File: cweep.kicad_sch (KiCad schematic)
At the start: 73 parts, among them J1 24AWG Hole, J2 24AWG Hole, SW1 SW_Push, SW10 SW_Push, SW11 SW_Push, SW12 SW_Push, SW13 SW_Push, SW14 SW_Push, SW15 SW_Push, SW16 SW_Push, SW17 SW_Push, SW18 SW_SPST, SW19 SW_Omron_B3FS, SW2 SW_Push, SW3 SW_Push, SW4 SW_Push, SW5 SW_Push, SW6 SW_Push, SW7 SW_Push, SW8 SW_Push, SW9 SW_Push, U1 XIAO-nRF52840, U2 BQ25504

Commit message: feat: add reversible inductor
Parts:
- LBST1: footprint Inductor_SMD:L_1210_3225Metric_Pad1.42x2.65mm_HandSolder -> cweep:L_1210_3225Metric_Pad1.42x2.65mm_HandSolder_Reversible
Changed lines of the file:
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@@
 			)
 		)
-		(property "Footprint" "Inductor_SMD:L_1210_3225Metric_Pad1.42x2.65mm_HandSolder"
+		(property "Footprint" "cweep:L_1210_3225Metric_Pad1.42x2.65mm_HandSolder_Reversible"
 			(at 46.99 36.83 0)
 			(effects

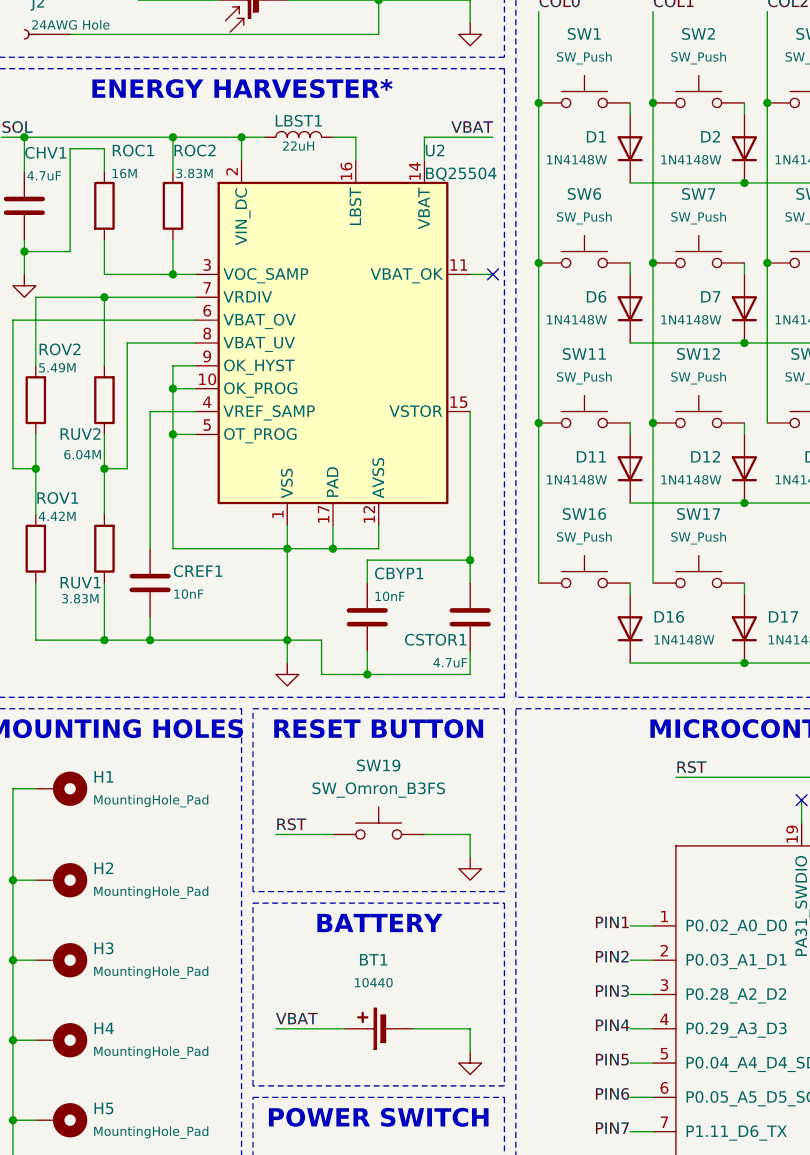
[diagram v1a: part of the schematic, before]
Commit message: refactor: 10440 -> ICR10440
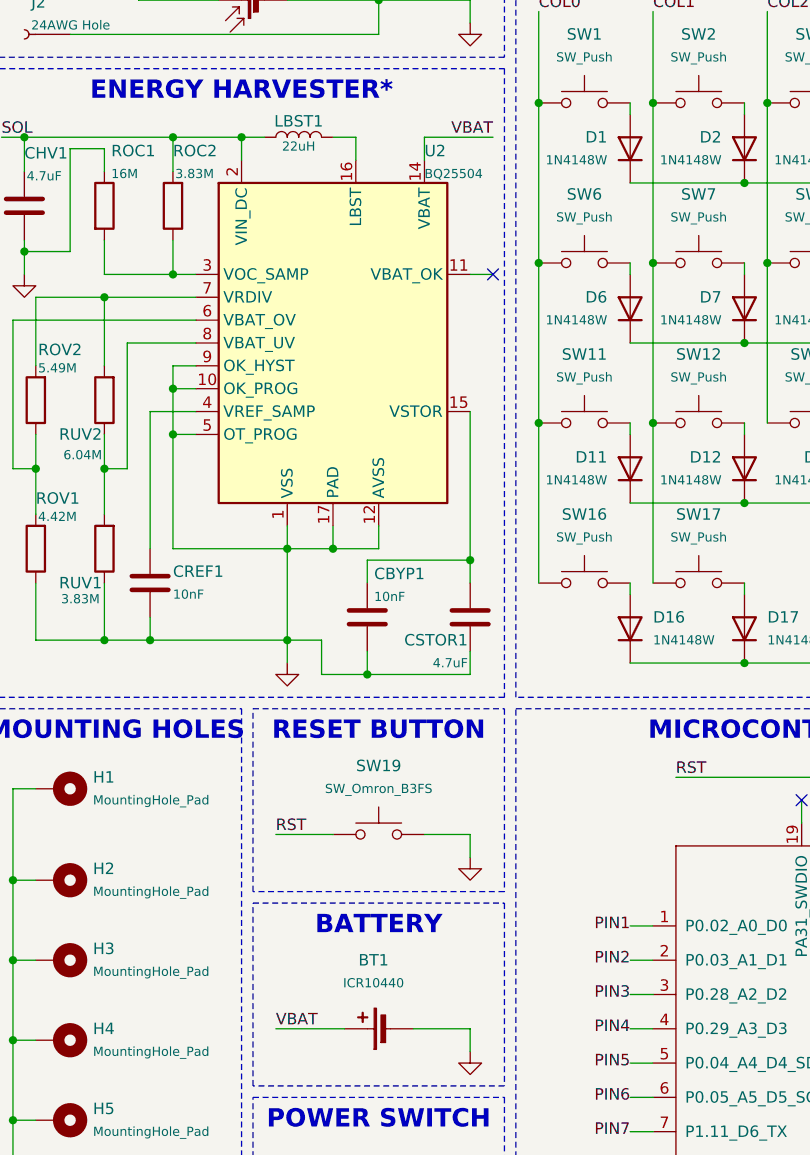
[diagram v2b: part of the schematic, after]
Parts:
- BT1: value 10440 -> ICR10440
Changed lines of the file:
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@@
 			)
 		)
-		(property "Value" "10440"
+		(property "Value" "ICR10440"
 			(at 55.3085 130.81 90)
 			(effects
@@
 			(effects
 				(font
-					(size 1.27 1.27)
+					(size 1.016 1.016)
 				)
 			)
@@
 			(effects
 				(font
-					(size 1.27 1.27)
-				)
-				(justify left)
+					(size 1.016 1.016)
+				)
+				(justify left)

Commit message: fix: correct footprint for inductor
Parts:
- LBST1: footprint cweep:L_1210_3225Metric_Pad1.42x2.65mm_HandSolder_Reversible -> cweep:L_Abracon_ASPI-4030S_Reversible
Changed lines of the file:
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@@
 			)
 		)
-		(property "Footprint" "cweep:L_1210_3225Metric_Pad1.42x2.65mm_HandSolder_Reversible"
+		(property "Footprint" "cweep:L_Abracon_ASPI-4030S_Reversible"
 			(at 46.99 36.83 0)
 			(effects

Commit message: fix: correct schematic footprint assignments
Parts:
- CBYP1, CHV1, CREF1, CSTOR1: footprint Capacitor_SMD:C_0603_1608Metric_Pad1.08x0.95mm_HandSolder -> cweep:C_0603_1608Metric_Pad1.08x0.95mm_HandSolder
- J1, J2: footprint Connector_Wire:SolderWire-0.127sqmm_1x01_D0.48mm_OD1mm_Relief -> cweep:SolderWire-0.127sqmm_1x01_D0.48mm_OD1mm_Relief
- ROC1, ROC2, ROV1, ROV2, RUV1, RUV2: footprint Resistor_SMD:R_0603_1608Metric_Pad0.98x0.95mm_HandSolder -> cweep:R_0603_1608Metric_Pad0.98x0.95mm_HandSolder
- SW19: footprint cweep:SW_TH_Tactile_Omron_B3F-10xx_Reversible -> cweep:SW_TH_Tactile_Omron_B3F-102x_Reversible
- U2: footprint Package_DFN_QFN:VQFN-16-1EP_3x3mm_P0.5mm_EP1.68x1.68mm -> cweep:VQFN-16-1EP_3x3mm_P0.5mm_EP1.68x1.68mm
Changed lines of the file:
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@@
 			)
 		)
-		(property "Footprint" "Resistor_SMD:R_0603_1608Metric_Pad0.98x0.95mm_HandSolder"
+		(property "Footprint" "cweep:R_0603_1608Metric_Pad0.98x0.95mm_HandSolder"
 			(at 34.798 44.45 90)
 			(effects
@@
 			)
 		)
-		(property "Footprint" "Resistor_SMD:R_0603_1608Metric_Pad0.98x0.95mm_HandSolder"
+		(property "Footprint" "cweep:R_0603_1608Metric_Pad0.98x0.95mm_HandSolder"
 			(at 27.178 82.55 90)
 			(effects
@@
 			)
 		)
-		(property "Footprint" "Resistor_SMD:R_0603_1608Metric_Pad0.98x0.95mm_HandSolder"
+		(property "Footprint" "cweep:R_0603_1608Metric_Pad0.98x0.95mm_HandSolder"
 			(at 19.558 82.55 90)
 			(effects
@@
 			)
 		)
-		(property "Footprint" "Capacitor_SMD:C_0603_1608Metric_Pad1.08x0.95mm_HandSolder"
+		(property "Footprint" "cweep:C_0603_1608Metric_Pad1.08x0.95mm_HandSolder"
 			(at 17.4752 48.26 0)
 			(effects
@@
 			)
 		)
-		(property "Footprint" "Connector_Wire:SolderWire-0.127sqmm_1x01_D0.48mm_OD1mm_Relief"
+		(property "Footprint" "cweep:SolderWire-0.127sqmm_1x01_D0.48mm_OD1mm_Relief"
 			(at 16.51 17.78 0)
 			(effects
@@
 			)
 		)
-		(property "Footprint" "Resistor_SMD:R_0603_1608Metric_Pad0.98x0.95mm_HandSolder"
+		(property "Footprint" "cweep:R_0603_1608Metric_Pad0.98x0.95mm_HandSolder"
 			(at 23.622 44.45 90)
 			(effects
@@
 			)
 		)
-		(property "Footprint" "cweep:SW_TH_Tactile_Omron_B3F-10xx_Reversible"
+		(property "Footprint" "cweep:SW_TH_Tactile_Omron_B3F-102x_Reversible"
 			(at 55.88 109.22 0)
 			(effects
@@
 			)
 		)
-		(property "Footprint" "Connector_Wire:SolderWire-0.127sqmm_1x01_D0.48mm_OD1mm_Relief"
+		(property "Footprint" "cweep:SolderWire-0.127sqmm_1x01_D0.48mm_OD1mm_Relief"
 			(at 16.51 25.4 0)
 			(effects
@@
 			)
 		)
-		(property "Footprint" "Capacitor_SMD:C_0603_1608Metric_Pad1.08x0.95mm_HandSolder"
+		(property "Footprint" "cweep:C_0603_1608Metric_Pad1.08x0.95mm_HandSolder"
 			(at 55.5752 93.98 0)
 			(effects
@@
 			)
 		)
-		(property "Footprint" "Resistor_SMD:R_0603_1608Metric_Pad0.98x0.95mm_HandSolder"
+		(property "Footprint" "cweep:R_0603_1608Metric_Pad0.98x0.95mm_HandSolder"
 			(at 27.178 66.04 90)
 			(effects
@@
 			)
 		)
-		(property "Footprint" "Package_DFN_QFN:VQFN-16-1EP_3x3mm_P0.5mm_EP1.68x1.68mm"
+		(property "Footprint" "cweep:VQFN-16-1EP_3x3mm_P0.5mm_EP1.68x1.68mm"
 			(at 50.8 59.69 0)
 			(effects
@@
 			)
 		)
-		(property "Footprint" "Capacitor_SMD:C_0603_1608Metric_Pad1.08x0.95mm_HandSolder"
+		(property "Footprint" "cweep:C_0603_1608Metric_Pad1.08x0.95mm_HandSolder"
 			(at 31.4452 90.17 0)
 			(effects
@@
 			)
 		)
-		(property "Footprint" "Resistor_SMD:R_0603_1608Metric_Pad0.98x0.95mm_HandSolder"
+		(property "Footprint" "cweep:R_0603_1608Metric_Pad0.98x0.95mm_HandSolder"
 			(at 19.558 66.04 90)
 			(effects
@@
 			)
 		)
-		(property "Footprint" "Capacitor_SMD:C_0603_1608Metric_Pad1.08x0.95mm_HandSolder"
+		(property "Footprint" "cweep:C_0603_1608Metric_Pad1.08x0.95mm_HandSolder"
 			(at 65.0748 93.98 0)
 			(effects

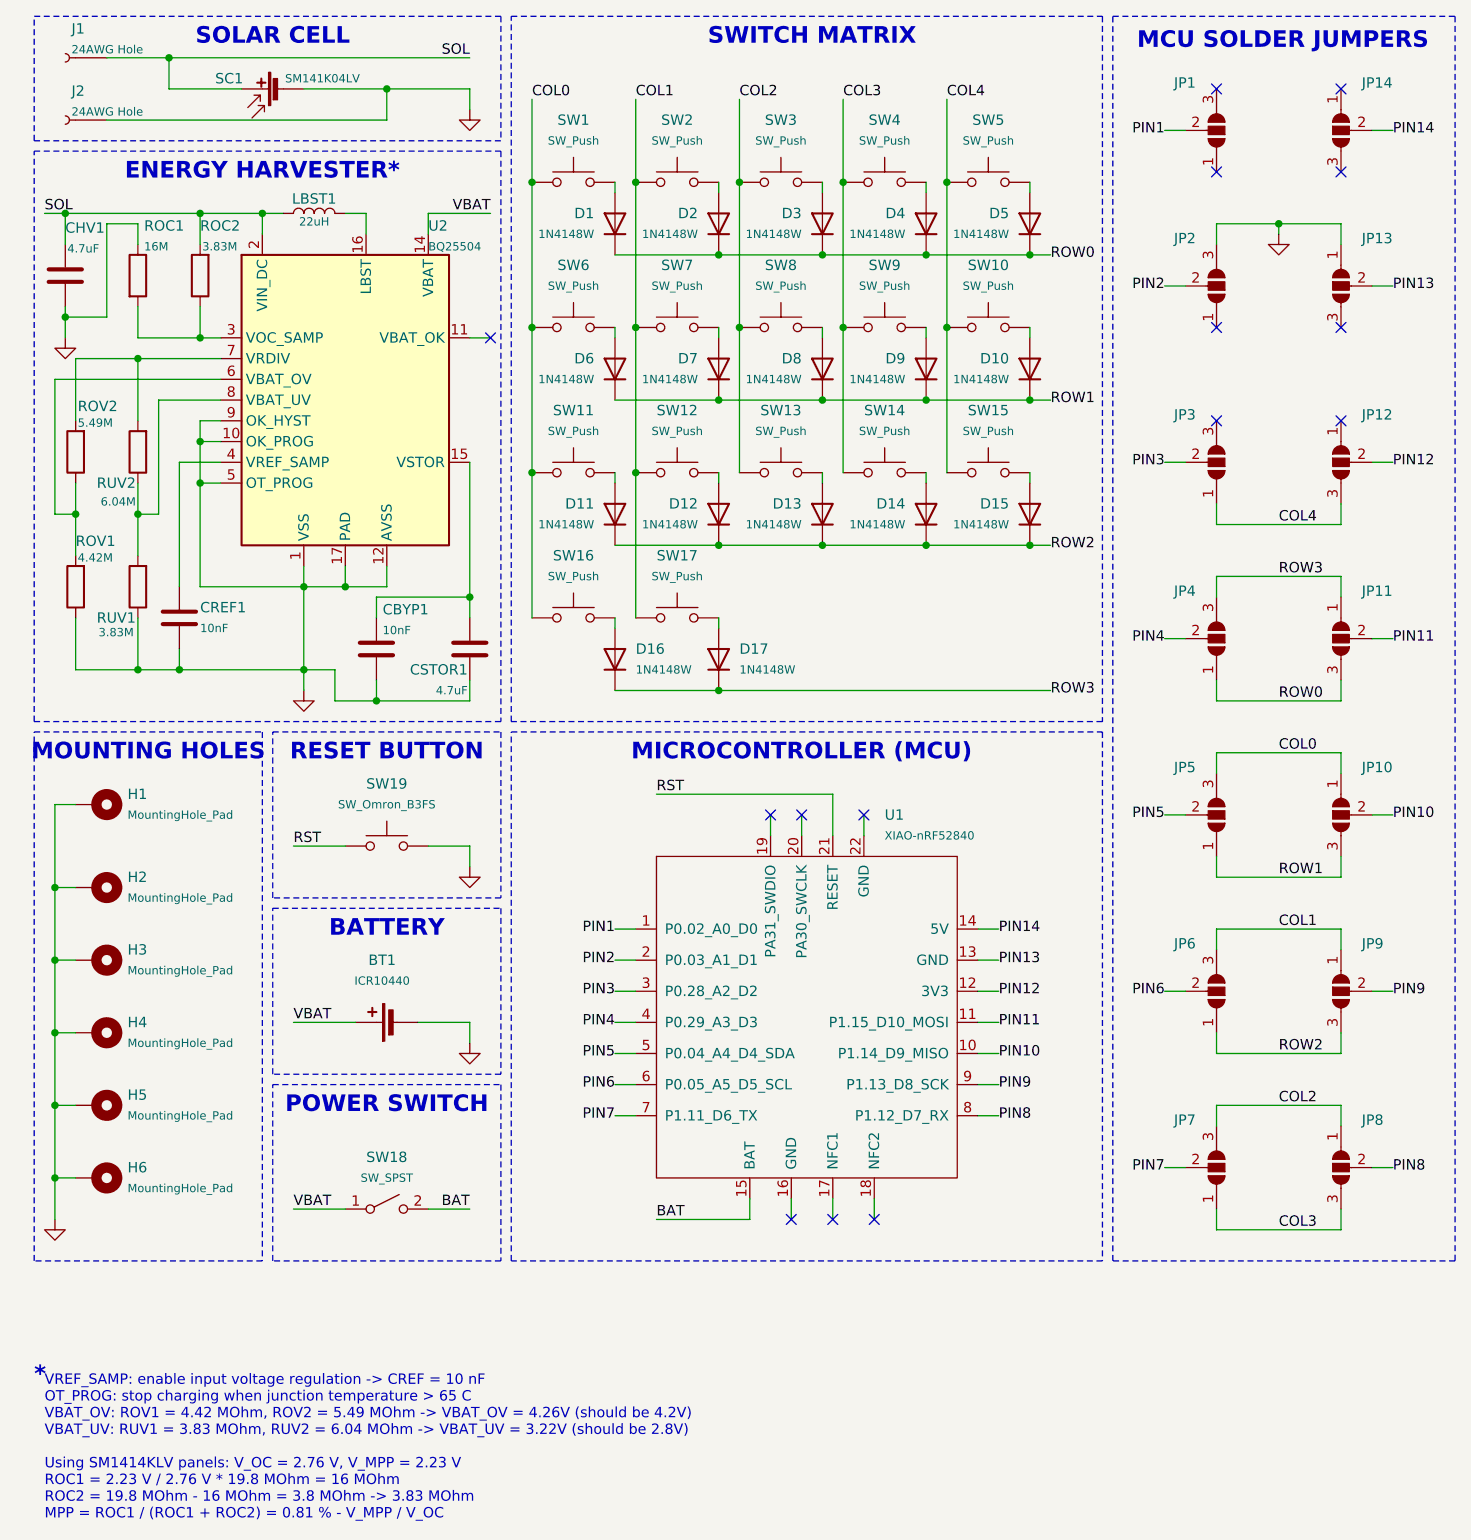
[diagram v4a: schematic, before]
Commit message: chore: update kicad from 9.0 to 10.0
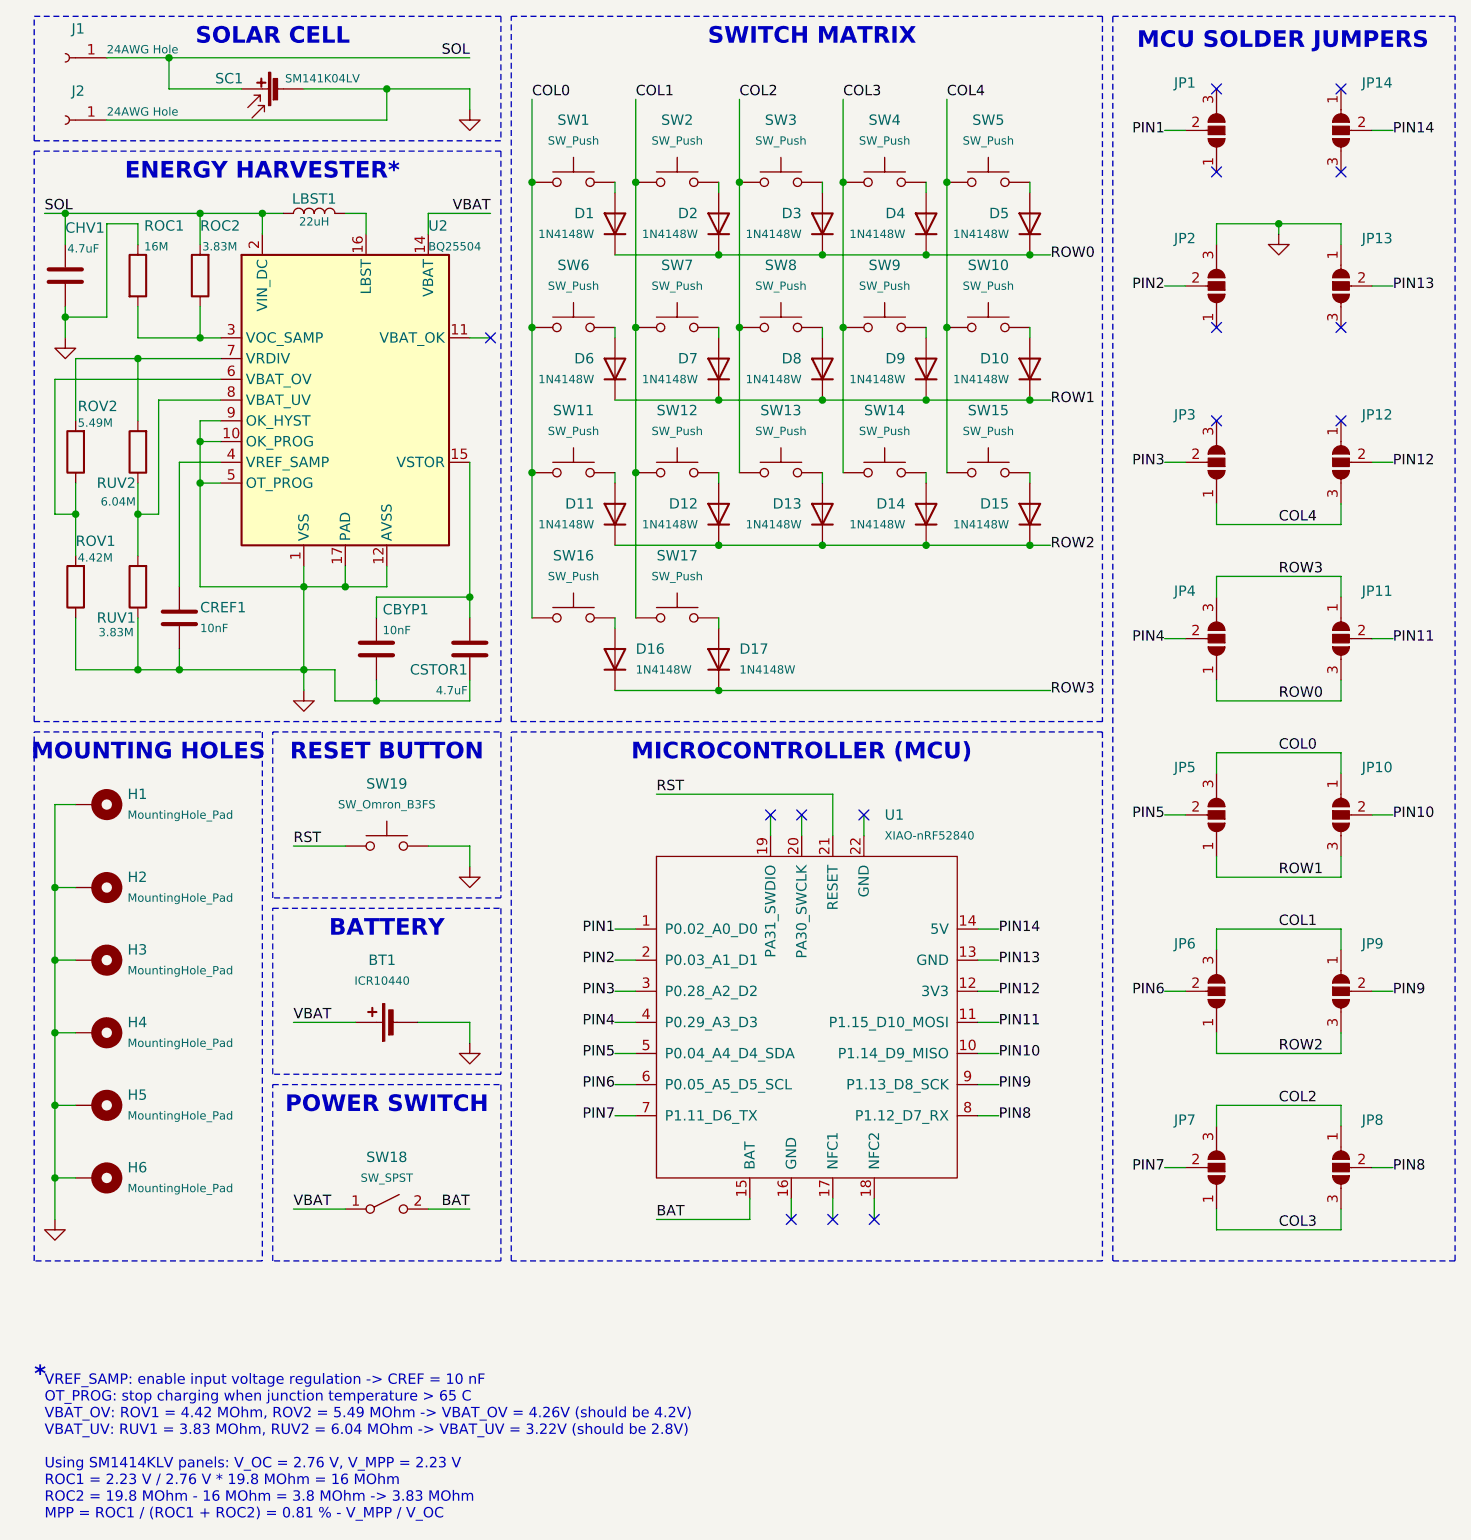
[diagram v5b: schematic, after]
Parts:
- D1, D10, D11, D12, D13, D14, D15, D16, D17, D2, D3, D4, D5, D6, D7, D8, D9: footprint cweep:D_SOD-123_Reversible -> Diode_SMD:D_SOD-123
- U2: footprint cweep:VQFN-16-1EP_3x3mm_P0.5mm_EP1.68x1.68mm -> Package_DFN_QFN:VQFN-16-1EP_3x3mm_P0.5mm_EP1.68x1.68mm
